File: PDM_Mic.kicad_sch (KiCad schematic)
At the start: 31 parts, among them J10 JST_SH_1x4_BM04B-SRSS-TB-LF-SN, J4 Conn_FFC_Molex_5019510550, J5 Conn_FFC_Molex_5019510550, U18 TPD4E05U06QDQARQ1, U19 TPD4E05U06QDQARQ1, U20 TLV73318PDBVT, U21 ADAU7118ACPZRL, U22 TPD4E02B04DQA

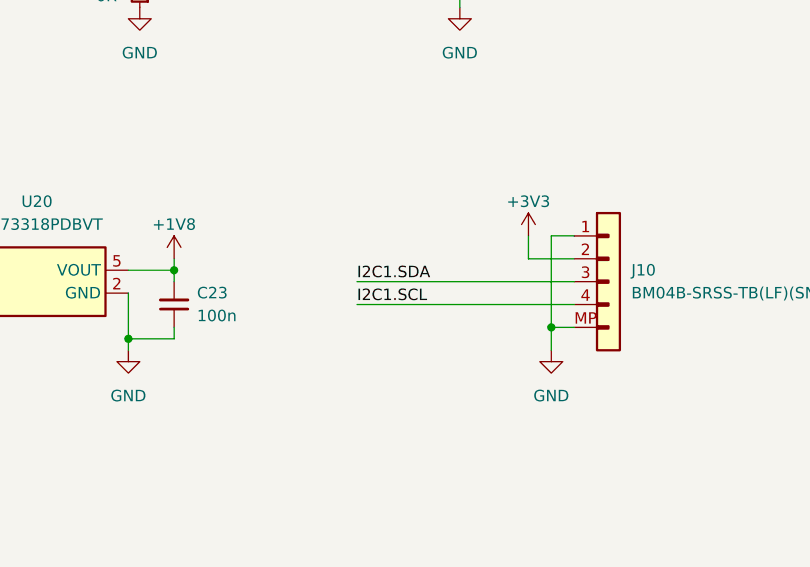
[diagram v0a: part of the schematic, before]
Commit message: [#71230] Fix I2C bus indexing
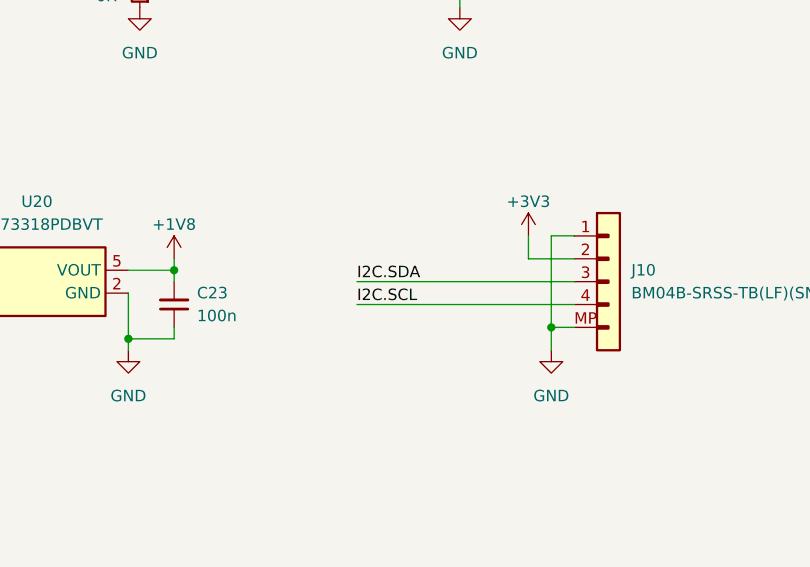
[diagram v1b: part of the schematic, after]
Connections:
- net I2C.SCL: now also J10.4
- net I2C.SDA: now also J10.3
- net I2C1.SCL: no longer J10.4
- net I2C1.SDA: no longer J10.3
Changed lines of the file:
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@@
 		)
 	)
-	(label "I2C1.SDA"
+	(label "I2C.SDA"
 		(at 256.54 187.96 0)
 		(fields_autoplaced yes)
@@
 		)
 	)
-	(label "I2C1.SCL"
+	(label "I2C.SCL"
 		(at 256.54 190.5 0)
 		(fields_autoplaced yes)

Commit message: [#71230] Import components to the PCB
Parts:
- removed U22: TPD4E02B04DQA, antmicro-footprints:USON-10_2.5x1mm_P0.5mm, symbol antmicroTVSDiodes:TPD4E02B04DQA
- added D10, D11, D9: TPD1E0B04_XDFN-2, antmicro-footprints:XDFN-2_1x0.60mm, symbol antmicroTVSDiodes:TPD1E0B04_XDFN-2
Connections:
- net +3V3: now also D9.2 (A)
- net GND: now also D10.1 (C), D11.1 (C), D9.1 (C)
- net I2C.SCL: now also D10.2 (A)
- net I2C.SDA: now also D11.2 (A)
- no-connect marks 6 -> 5

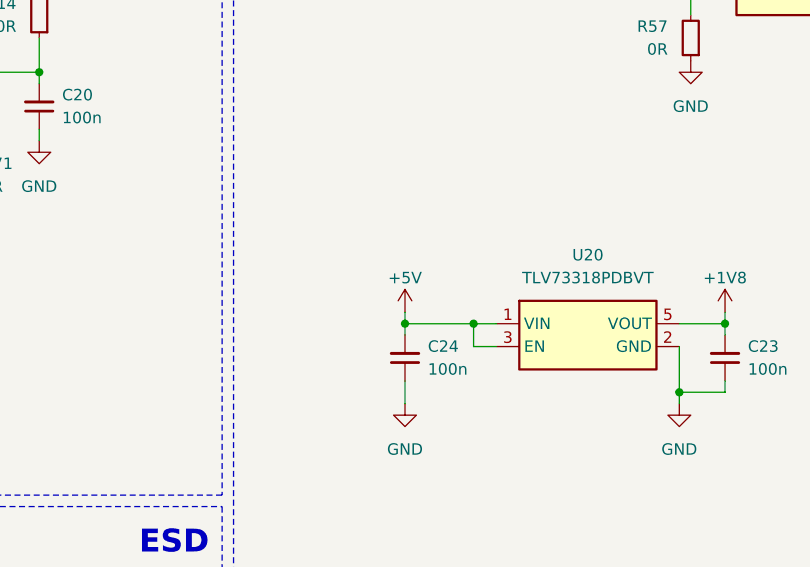
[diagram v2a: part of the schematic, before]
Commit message: [#72130] Change 1V8 LDO to power from 3V3, improve power planes
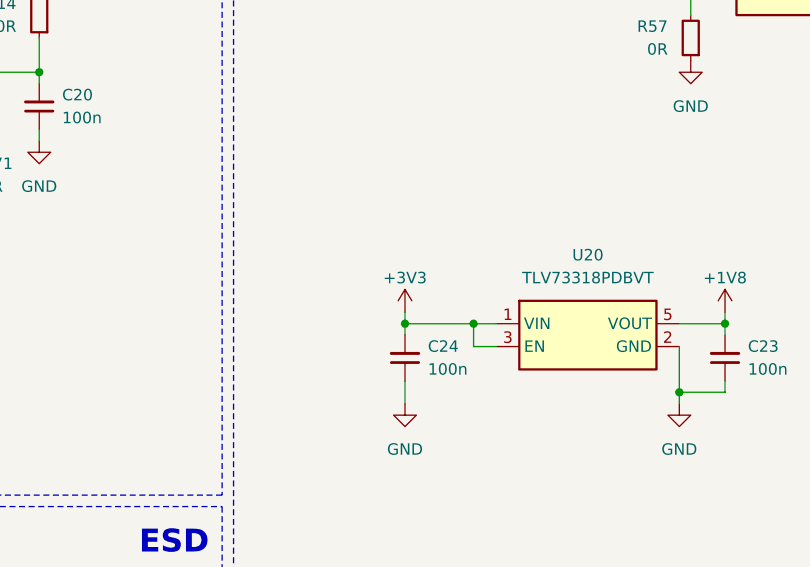
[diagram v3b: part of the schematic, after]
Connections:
- net +5V is gone; now on net +3V3: C24.2, U20.1 (VIN), U20.3 (EN)
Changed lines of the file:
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@@
-	)
-	(symbol
-		(lib_id "antmicropower:+5V")
-		(at 200.66 185.42 0)
-		(unit 1)
-		(exclude_from_sim no)
-		(in_bom yes)
-		(on_board yes)
-		(dnp no)
-		(property "Reference" "#PWR0137"
-			(at 215.9 187.96 0)
-			(effects
-				(font
-					(size 1.27 1.27)
-					(thickness 0.15)
-				)
-				(justify left bottom)
-				(hide yes)
-			)
-		)
-		(property "Value" "+5V"
-			(at 200.66 181.61 0)
-			(effects
-				(font
-					(size 1.27 1.27)
-					(thickness 0.15)
-				)
-			)
-		)
-		(property "Footprint" ""
-			(at 215.9 193.04 0)
-			(effects
-				(font
-					(size 1.27 1.27)
-					(thickness 0.15)
-				)
-				(justify left bottom)
-				(hide yes)
-			)
-		)
-		(property "Datasheet" ""
-			(at 215.9 195.58 0)
-			(effects
-				(font
-					(size 1.27 1.27)
-					(thickness 0.15)
-				)
-				(justify left bottom)
-				(hide yes)
-			)
-		)
-		(property "Description" ""
-			(at 200.66 185.42 0)
-			(effects
-				(font
-					(size 1.27 1.27)
-				)
-				(hide yes)
-			)
-		)
-		(property "Author" "Antmicro"
-			(at 215.9 193.04 0)
-			(effects
-				(font
-					(size 1.27 1.27)
-					(thickness 0.15)
-				)
-				(justify left bottom)
-				(hide yes)
-			)
-		)
-		(property "License" "Apache-2.0"
-			(at 215.9 195.58 0)
-			(effects
-				(font
-					(size 1.27 1.27)
-					(thickness 0.15)
-				)
-				(justify left bottom)
-				(hide yes)
-			)
-		)
-		(pin "1"
-		)
-		(instances
-			(project ""
-				(path "/7fb12ebf-f685-4412-b638-445b1bf344bc/40ac334b-c599-49c0-9e0c-ed974f127645"
-					(reference "#PWR0137")
-					(unit 1)
-				)
-			)
-		)
 	)
 	(symbol
@@
 					(unit 1)
 				)
+			)
+		)
+	)
+	(symbol
+		(lib_id "antmicropower:+3V3")
+		(at 200.66 185.42 0)
+		(unit 1)
+		(exclude_from_sim no)
+		(in_bom yes)
+		(on_board yes)
+		(dnp no)
+		(property "Reference" "#PWR0146"
+			(at 215.9 185.42 0)
+			(effects
+				(font
+					(size 1.27 1.27)
+					(thickness 0.15)
+				)
+				(justify left bottom)
+				(hide yes)
+			)
+		)
+		(property "Value" "+3V3"
+			(at 200.66 181.61 0)
+			(effects
+				(font
+					(size 1.27 1.27)
+					(thickness 0.15)
+				)
+			)
+		)
+		(property "Footprint" ""
+			(at 215.9 193.04 0)
+			(effects
+				(font
+					(size 1.27 1.27)
+					(thickness 0.15)
+				)
+				(justify left bottom)
+				(hide yes)
+			)
+		)
+		(property "Datasheet" ""
+			(at 215.9 195.58 0)
+			(effects
+				(font
+					(size 1.27 1.27)
+					(thickness 0.15)
+				)
+				(justify left bottom)
+				(hide yes)
+			)
+		)
+		(property "Description" ""
+			(at 200.66 185.42 0)
+			(effects
+				(font
+					(size 1.27 1.27)
+				)
+				(hide yes)
+			)
+		)
+		(property "Author" "Antmicro"
+			(at 215.9 187.96 0)
+			(effects
+				(font
+					(size 1.27 1.27)
+					(thickness 0.15)
+				)
+				(justify left bottom)
+				(hide yes)
+			)
+		)
+		(property "License" "Apache-2.0"
+			(at 215.9 190.5 0)
+			(effects
+				(font
+					(size 1.27 1.27)
+					(thickness 0.15)
+				)
+				(justify left bottom)
+				(hide yes)
+			)
+		)
+		(pin "1"
+		)
+		(instances
+			(project "audio-controller-board"
+				(path "/7fb12ebf-f685-4412-b638-445b1bf344bc/40ac334b-c599-49c0-9e0c-ed974f127645"
+					(reference "#PWR0146")
+					(unit 1)
+				)
